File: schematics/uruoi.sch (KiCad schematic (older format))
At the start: 11 parts, among them U1 NJU7223F33, U2 ESP-WROOM-02, U3 MCP3002, U4 Soil_Moisture_Sensor

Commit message: docs: update schematics
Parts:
- added BT2: Mobile Battery (5V), symbol Device:Battery_Cell
- added M1: Pump, symbol Motor:Pump
- added R5: 270Ω, symbol Device:R
- added U5: TLP222A, Package_DIP:DIP-4_W7.62mm, symbol Relay_SolidState:TLP222A
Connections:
- net GND: now also U5.2
- net at U3.1 (~CS~/SHDN): now also R4.1, U2.6 (IO15); no longer U2.14 (IO5)
- new net: BT2.1 (+), M1.1 (+)
- new net: M1.2 (-), U5.4
- new net: BT2.2 (-), U5.3
- new net: R5.1, U5.1
- new net WATERING: R5.2, U2.14 (IO5)
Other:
- moved on the sheet: BT1, C1, C2, R1, R2, R3, R4, U1, U2, U3, U4

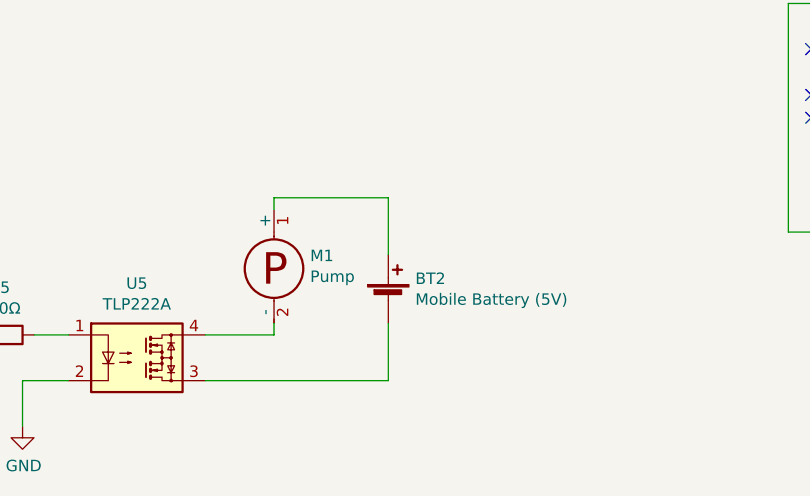
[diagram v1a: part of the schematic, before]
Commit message: feat: add a switch to water manually
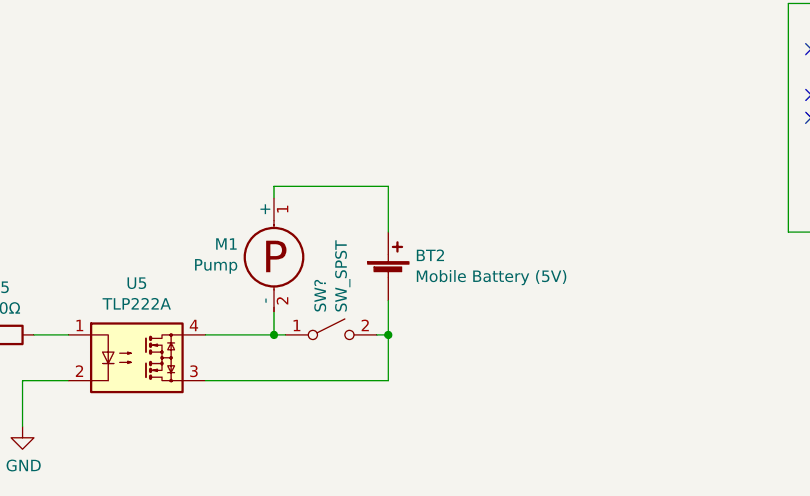
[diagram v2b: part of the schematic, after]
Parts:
- added SW?: SW_SPST, symbol Switch:SW_SPST
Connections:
- net at M1.2 (-), U5.4: now also SW?.1 (A)
- net at BT2.2 (-), U5.3: now also SW?.2 (B)
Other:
- moved on the sheet: BT2, M1
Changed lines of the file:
@@
 $EndComp
 Wire Wire Line
-	3800 5200 3800 4950
+	3800 5200 3800 5000
 Wire Wire Line
 	3000 5200 3800 5200
 Wire Wire Line
-	3300 4400 3300 4450
+	3300 4350 3300 4400
 Wire Wire Line
-	3800 4400 3300 4400
+	3800 4350 3300 4350
 Wire Wire Line
-	3800 4650 3800 4400
+	3800 4550 3800 4350
 Wire Wire Line
-	3300 5000 3300 4950
+	3300 5000 3300 4900
 Wire Wire Line
 	3000 5000 3300 5000
@@
 L Device:Battery_Cell BT2
 U 1 1 60D3A61D
-P 3800 4850
-F 0 "BT2" H 3918 4946 50  0000 L CNN
-F 1 "Mobile Battery (5V)" H 3918 4855 50  0000 L CNN
-F 2 "" V 3800 4910 50  0001 C CNN
-F 3 "~" V 3800 4910 50  0001 C CNN
-	1    3800 4850
+P 3800 4750
+F 0 "BT2" H 3918 4846 50  0000 L CNN
+F 1 "Mobile Battery (5V)" H 3918 4755 50  0000 L CNN
+F 2 "" V 3800 4810 50  0001 C CNN
+F 3 "~" V 3800 4810 50  0001 C CNN
+	1    3800 4750
 	1    0    0    -1
 $EndComp
@@
 L Motor:Pump M1
 U 1 1 60D39908
-P 3300 4700
-F 0 "M1" H 3458 4746 50  0000 L CNN
-F 1 "Pump" H 3458 4655 50  0000 L CNN
-F 2 "" H 3300 4700 50  0001 C CNN
-F 3 "" H 3300 4700 50  0001 C CNN
-	1    3300 4700
+P 3300 4650
+F 0 "M1" H 3143 4696 50  0000 R CNN
+F 1 "Pump" H 3143 4605 50  0000 R CNN
+F 2 "" H 3300 4650 50  0001 C CNN
+F 3 "" H 3300 4650 50  0001 C CNN
+	1    3300 4650
 	1    0    0    -1
 $EndComp
+$Comp
+L Switch:SW_SPST SW?
+U 1 1 60DD3E0C
+P 3550 5000
+F 0 "SW?" V 3504 5098 50  0000 L CNN
+F 1 "SW_SPST" V 3595 5098 50  0000 L CNN
+F 2 "" H 3550 5000 50  0001 C CNN
+F 3 "~" H 3550 5000 50  0001 C CNN
+	1    3550 5000
+	1    0    0    -1
+$EndComp
+Wire Wire Line
+	3350 5000 3300 5000
+Connection ~ 3300 5000
+Wire Wire Line
+	3750 5000 3800 5000
+Connection ~ 3800 5000
+Wire Wire Line
+	3800 5000 3800 4850
 $EndSCHEMATC
